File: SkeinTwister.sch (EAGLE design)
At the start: 14 parts, among them U1 TSR_1-2450

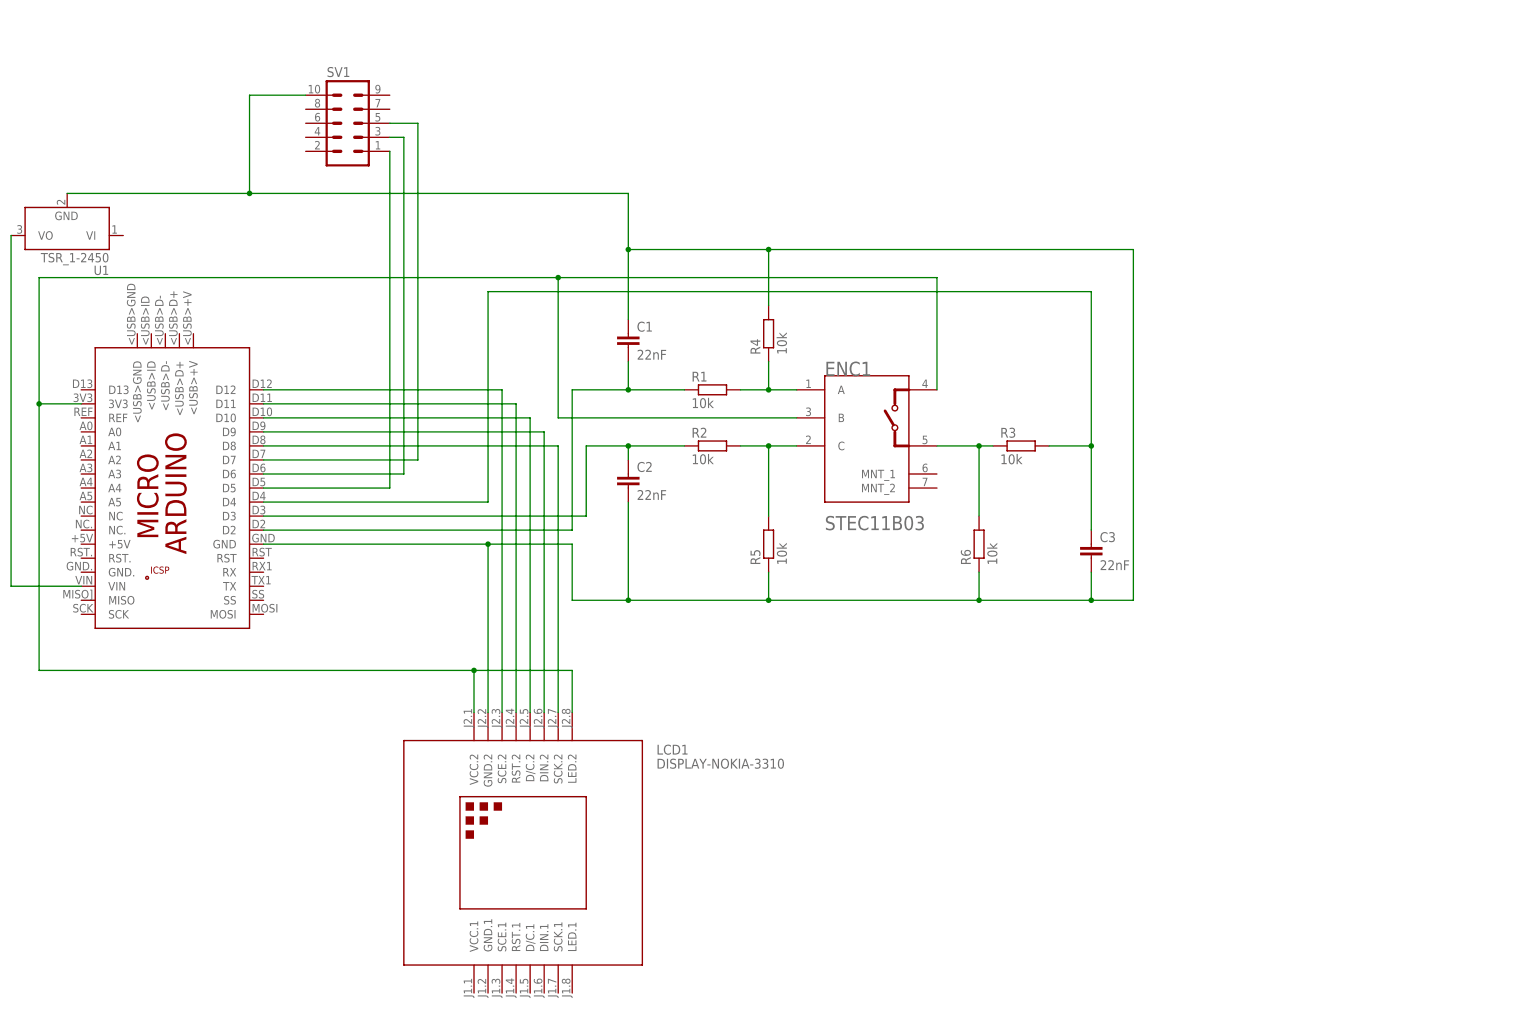
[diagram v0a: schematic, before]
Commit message: Redone schematics after first test
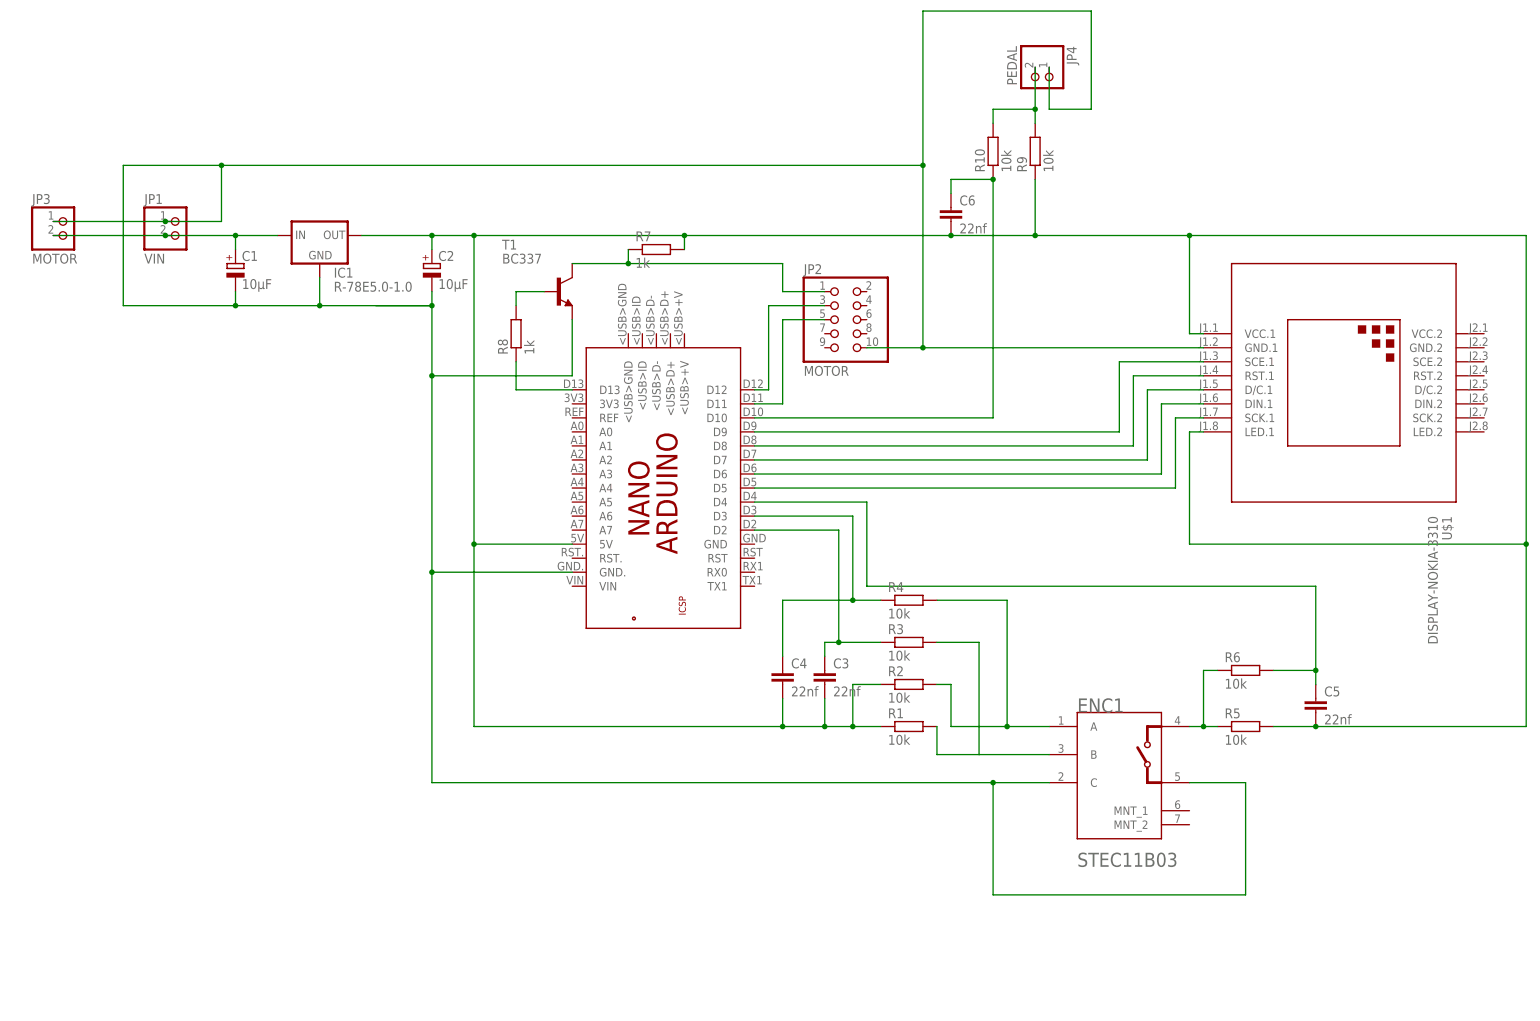
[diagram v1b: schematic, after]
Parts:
- removed LCD1: DISPLAY-NOKIA-3310, diy-modules:DISPLAY-NOKIA-3310
- removed PCB1: ARDUINO_MICRO, E14_Arduino_revC:ARDUINO_MICRO
- removed SV1: (no value), con-ml:ML10
- removed U1: TSR_1-2450, _traco_tsr-1:TSR_1-2450
- added C4, C5, C6: 22nf, rcl:C-EU025-024X044
- added IC1: R-78E5.0-1.0, r-78xx_10:R-78E5.0-1.0
- added JP1: VIN, pinhead:PINHD-1X2
- added JP2: MOTOR, pinhead:PINHD-2X5
- added JP3: MOTOR, pinhead:PINHD-1X2
- added JP4: PEDAL, pinhead:PINHD-1X2
- added PCB2: ARDUINO_NANO, E14_Arduino_revC:ARDUINO_NANO
- added R10, R9: 10k, rcl:R-EU_0204/5
- added R7, R8: 1k, rcl:R-EU_0204/5
- added T1: BC337, transistor:BC337
- added U$1: DISPLAY-NOKIA-3310, diy-modules:DISPLAY-NOKIA-3310
- C1, C2: value 22nF -> 10µF; device rcl:C-EU050-050X075 -> rcl:CPOL-EUE5-5
- C3: value 22nF -> 22nf; device rcl:C-EU050-050X075 -> rcl:C-EU025-024X044
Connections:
- new net N$18: PCB2.D8, U$1.RST.1
- new net N$19: PCB2.D9, U$1.SCE.1
- new net N$20: JP4.2, R10.2, R9.2
- new net N$21: C6.1, PCB2.D10, R10.1
- net N$1: now also C1.+, IC1.IN, JP1.2, JP3.2; no longer ENC1.A, R1.2, R4.1
- net N$10: now also JP2.3, PCB2.D12; no longer LCD1.RST.2, PCB1.D11
- net N$11: now also JP2.5, PCB2.D11; no longer LCD1.D/C.2, PCB1.D10
- net N$12: now also PCB2.D13, R8.1; no longer LCD1.DIN.2, PCB1.D9
- net N$13: now also R8.2, T1.B; no longer LCD1.SCK.2, PCB1.D8
- net N$14: now also JP2.1, R7.1, T1.C; no longer PCB1.VIN, U1.VO
- net N$15: now also C1.-, C2.-, ENC1.5, ENC1.C, IC1.GND, JP1.1, JP2.10, JP3.1, JP4.1, PCB2.GND., T1.E, U$1.GND.1; no longer PCB1.D5, SV1.1
- net N$16: now also PCB2.D6, U$1.DIN.1; no longer PCB1.D6, SV1.3
- net N$17: now also PCB2.D7, U$1.D/C.1; no longer PCB1.D7, SV1.5
- net N$2: now also PCB2.D5, U$1.SCK.1; no longer ENC1.C, R2.2, R5.2
- net N$3: now also C2.+, C3.2, C4.2, C5.2, C6.2, IC1.OUT, PCB2.5V, R1.1, R2.1, R5.2, R7.2, R9.1, U$1.LED.1, U$1.VCC.1; no longer ENC1.5, R3.1, R6.2
- net N$4: now also ENC1.B, R1.2; no longer C3.1, PCB1.D4
- net N$5: now also ENC1.A, R2.2; no longer C1.1, C2.2, C3.2, LCD1.GND.2, PCB1.GND, R5.1, R6.1, SV1.10, U1.GND
- net N$6: now also C5.1, PCB2.D4, R6.2; no longer C2.1, PCB1.D3, R2.1
- net N$7: now also C3.1, PCB2.D2, R3.1; no longer C1.2, PCB1.D2, R1.1
- net N$8: now also C4.1, PCB2.D3, R4.1; no longer LCD1.SCE.2, PCB1.D12
- net N$9: now also R5.1, R6.1; no longer ENC1.B, LCD1.LED.2, LCD1.VCC.2, PCB1.3V3, PCB1.<USB>GND
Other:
- moved on the sheet: C3, ENC1, R1, R2, R3, R4, R5, R6

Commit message: Fix of schematics after protoype
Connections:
- new net N$22: PCB2.3V3, U$1.LED.1, U$1.VCC.1
- net N$15: now also C3.2, C4.2, C5.2, C6.2
- net N$3: no longer C3.2, C4.2, C5.2, C6.2, U$1.LED.1, U$1.VCC.1
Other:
- moved on the sheet: C5, C6, R10, R6, R9
